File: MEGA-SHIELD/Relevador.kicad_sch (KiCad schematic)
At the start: 8 parts, among them J2 Conn_01x03_Female, J4 Screw_Terminal_01x04, K1 G5LE-1, Q1 2N7002H

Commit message: feat: cambios
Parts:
- R1: value 330 -> 1k
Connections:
- net sig: now reaches Q1.1 (G), R1.1, R3.1
- net 12V renamed +12V
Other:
- note removed: "aqui va el pin que usare para activar el relevador"
- moved on the sheet: D1, R1
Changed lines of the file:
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@@
 (kicad_sch (version 20230121) (generator eeschema)
   (paper "A4")
+  (junction (at 130.048 105.156) (diameter 0) (color 0 0 0 0)
+  )
   (junction (at 137.668 110.998) (diameter 0) (color 0 0 0 0)
   )
@@
   (junction (at 130.048 110.998) (diameter 0) (color 0 0 0 0)
   )
-  (junction (at 163.068 100.076) (diameter 0) (color 0 0 0 0)
-  )
-  (wire (pts (xy 101.6 110.998) (xy 106.172 110.998))
+  (wire (pts (xy 130.048 132.842) (xy 130.048 128.27))
     (stroke (width 0) (type default))
   )
@@
     (stroke (width 0) (type default))
   )
-  (wire (pts (xy 113.792 110.998) (xy 115.824 110.998))
+  (wire (pts (xy 127.254 105.156) (xy 130.048 105.156))
+    (stroke (width 0) (type default))
+  )
+  (wire (pts (xy 130.048 120.65) (xy 130.048 118.618))
     (stroke (width 0) (type default))
   )
@@
     (stroke (width 0) (type default))
   )
-  (wire (pts (xy 137.668 110.998) (xy 137.668 113.792))
+  (wire (pts (xy 137.668 110.998) (xy 137.668 132.08))
     (stroke (width 0) (type default))
   )
@@
     (stroke (width 0) (type default))
   )
-  (wire (pts (xy 123.444 110.998) (xy 130.048 110.998))
-    (stroke (width 0) (type default))
-  )
   (wire (pts (xy 142.748 81.788) (xy 142.748 87.122))
     (stroke (width 0) (type default))
   )
-  (wire (pts (xy 163.068 100.076) (xy 166.878 100.076))
-    (stroke (width 0) (type default))
-  )
   (wire (pts (xy 144.526 107.696) (xy 144.526 100.076))
     (stroke (width 0) (type default))
   )
-  (text "aqui va el pin que usare para activar el relevador "
-    (at 83.566 103.378 0)
-    (effects (font (size 1.27 1.27)) (justify left bottom))
-  )
-  (text "Relevador\n" (at 143.764 120.65 0)
+  (text "Relevador\n" (at 150.368 122.428 0)
     (effects (font (size 1.27 1.27) bold) (justify left bottom))
   )
-  (label "5v" (at 166.878 100.076 0) (fields_autoplaced)
-    (effects (font (size 1.27 1.27)) (justify left bottom))
-  )
-  (global_label "12V" (shape output) (at 142.748 81.788 180) (fields_autoplaced)
+  (hierarchical_label "sig" (shape input) (at 127.254 105.156 180) (fields_autoplaced)
     (effects (font (size 1.27 1.27)) (justify right))
-    (property "Intersheetrefs" "${INTERSHEET_REFS}" (at 136.3346 81.788 0)
-      (effects (font (size 1.27 1.27)) (justify right) hide)
-    )
-  )
-  (global_label "GND" (shape output) (at 101.6 110.998 180) (fields_autoplaced)
-    (effects (font (size 1.27 1.27)) (justify right))
-    (property "Intersheetrefs" "${INTERSHEET_REFS}" (at 94.8237 110.998 0)
-      (effects (font (size 1.27 1.27)) (justify right) hide)
-    )
-  )
-  (global_label "GND" (shape output) (at 172.974 101.346 0) (fields_autoplaced)
+  )
+  (hierarchical_label "5v" (shape input) (at 163.068 100.076 0) (fields_autoplaced)
     (effects (font (size 1.27 1.27)) (justify left))
-    (property "Intersheetrefs" "${INTERSHEET_REFS}" (at 179.7503 101.346 0)
-      (effects (font (size 1.27 1.27)) (justify left) hide)
-    )
-  )
-  (global_label "GND" (shape output) (at 137.668 113.792 0) (fields_autoplaced)
-    (effects (font (size 1.27 1.27)) (justify left))
-    (property "Intersheetrefs" "${INTERSHEET_REFS}" (at 144.4443 113.792 0)
-      (effects (font (size 1.27 1.27)) (justify left) hide)
+  )
+  (symbol (lib_id "power:GND") (at 130.048 132.842 0) (unit 1)
+    (in_bom yes) (on_board yes) (dnp no) (fields_autoplaced)
+    (property "Reference" "#PWR04" (at 130.048 139.192 0)
+      (effects (font (size 1.27 1.27)) hide)
+    )
+    (property "Value" "GND" (at 130.048 137.414 0)
+      (effects (font (size 1.27 1.27)))
+    )
+    (property "Footprint" "" (at 130.048 132.842 0)
+      (effects (font (size 1.27 1.27)) hide)
+    )
+    (property "Datasheet" "" (at 130.048 132.842 0)
+      (effects (font (size 1.27 1.27)) hide)
+    )
+    (pin "1")
+    (instances
+      (project "ER-PROMEGA-SHIELD"
+        (path "/8147067b-5845-4831-8ba1-364ec5fe594c/4fd23662-bc02-400a-9352-be1f3c09ed5b"
+          (reference "#PWR04") (unit 1)
+        )
+      )
     )
   )
@@
     )
   )
+  (symbol (lib_id "power:GND") (at 172.974 101.346 0) (unit 1)
+    (in_bom yes) (on_board yes) (dnp no) (fields_autoplaced)
+    (property "Reference" "#PWR02" (at 172.974 107.696 0)
+      (effects (font (size 1.27 1.27)) hide)
+    )
+    (property "Value" "GND" (at 172.974 106.68 0)
+      (effects (font (size 1.27 1.27)))
+    )
+    (property "Footprint" "" (at 172.974 101.346 0)
+      (effects (font (size 1.27 1.27)) hide)
+    )
+    (property "Datasheet" "" (at 172.974 101.346 0)
+      (effects (font (size 1.27 1.27)) hide)
+    )
+    (pin "1")
+    (instances
+      (project "ER-PROMEGA-SHIELD"
+        (path "/8147067b-5845-4831-8ba1-364ec5fe594c/4fd23662-bc02-400a-9352-be1f3c09ed5b"
+          (reference "#PWR02") (unit 1)
+        )
+      )
+    )
+  )
   (symbol (lib_id "Connector:Screw_Terminal_01x04") (at 178.054 89.916 0) (unit 1)
     (in_bom yes) (on_board yes) (dnp no)
@@
     )
   )
-  (symbol (lib_id "Device:R_US") (at 119.634 110.998 270) (unit 1)
-    (in_bom yes) (on_board yes) (dnp no)
-    (property "Reference" "R1" (at 118.364 107.95 90)
-      (effects (font (size 1.27 1.27)) (justify left))
-    )
-    (property "Value" "330" (at 118.11 105.156 90)
-      (effects (font (size 1.27 1.27)) (justify left))
-    )
-    (property "Footprint" "Resistor_SMD:R_0805_2012Metric_Pad1.20x1.40mm_HandSolder" (at 119.38 112.014 90)
-      (effects (font (size 1.27 1.27)) hide)
-    )
-    (property "Datasheet" "~" (at 119.634 110.998 0)
+  (symbol (lib_id "power:+12V") (at 142.748 81.788 0) (unit 1)
+    (in_bom yes) (on_board yes) (dnp no) (fields_autoplaced)
+    (property "Reference" "#PWR01" (at 142.748 85.598 0)
+      (effects (font (size 1.27 1.27)) hide)
+    )
+    (property "Value" "+12V" (at 142.748 76.454 0)
+      (effects (font (size 1.27 1.27)))
+    )
+    (property "Footprint" "" (at 142.748 81.788 0)
+      (effects (font (size 1.27 1.27)) hide)
+    )
+    (property "Datasheet" "" (at 142.748 81.788 0)
+      (effects (font (size 1.27 1.27)) hide)
+    )
+    (pin "1")
+    (instances
+      (project "ER-PROMEGA-SHIELD"
+        (path "/8147067b-5845-4831-8ba1-364ec5fe594c/4fd23662-bc02-400a-9352-be1f3c09ed5b"
+          (reference "#PWR01") (unit 1)
+        )
+      )
+    )
+  )
+  (symbol (lib_id "Device:R_US") (at 130.048 114.808 0) (unit 1)
+    (in_bom yes) (on_board yes) (dnp no)
+    (property "Reference" "R1" (at 124.714 113.284 0)
+      (effects (font (size 1.27 1.27)) (justify left))
+    )
+    (property "Value" "1k" (at 124.968 115.316 0)
+      (effects (font (size 1.27 1.27)) (justify left))
+    )
+    (property "Footprint" "Resistor_SMD:R_0805_2012Metric_Pad1.20x1.40mm_HandSolder" (at 131.064 115.062 90)
+      (effects (font (size 1.27 1.27)) hide)
+    )
+    (property "Datasheet" "~" (at 130.048 114.808 0)
       (effects (font (size 1.27 1.27)) hide)
     )
@@
     )
   )
-  (symbol (lib_id "Device:LED") (at 109.982 110.998 0) (unit 1)
-    (in_bom yes) (on_board yes) (dnp no)
-    (property "Reference" "D1" (at 109.22 107.696 0)
+  (symbol (lib_id "Device:LED") (at 130.048 124.46 90) (unit 1)
+    (in_bom yes) (on_board yes) (dnp no)
+    (property "Reference" "D1" (at 123.952 123.19 90)
       (effects (font (size 1.27 1.27)) (justify right))
     )
-    (property "Value" "LEDRELE" (at 112.014 115.57 0)
+    (property "Value" "LEDRELE" (at 120.396 125.984 90)
       (effects (font (size 1.27 1.27)) (justify right))
     )
-    (property "Footprint" "LED_SMD:LED_1206_3216Metric_Pad1.42x1.75mm_HandSolder" (at 109.982 110.998 0)
-      (effects (font (size 1.27 1.27)) hide)
-    )
-    (property "Datasheet" "~" (at 109.982 110.998 0)
+    (property "Footprint" "LED_SMD:LED_1206_3216Metric_Pad1.42x1.75mm_HandSolder" (at 130.048 124.46 0)
+      (effects (font (size 1.27 1.27)) hide)
+    )
+    (property "Datasheet" "~" (at 130.048 124.46 0)
       (effects (font (size 1.27 1.27)) hide)
     )
@@
         )
       )
+    )
+  )
+  (symbol (lib_id "power:GND") (at 137.668 132.08 0) (unit 1)
+    (in_bom yes) (on_board yes) (dnp no) (fields_autoplaced)
+    (property "Reference" "#PWR03" (at 137.668 138.43 0)
+      (effects (font (size 1.27 1.27)) hide)
+    )
+    (property "Value" "GND" (at 137.668 136.906 0)
+      (effects (font (size 1.27 1.27)))
+    )
+    (property "Footprint" "" (at 137.668 132.08 0)
+      (effects (font (size 1.27 1.27)) hide)
+    )
+    (property "Datasheet" "" (at 137.668 132.08 0)
+      (effects (font (size 1.27 1.27)) hide)
+    )
+    (pin "1")
+    (instances
+      (project "ER-PROMEGA-SHIELD"
+        (path "/8147067b-5845-4831-8ba1-364ec5fe594c/4fd23662-bc02-400a-9352-be1f3c09ed5b"
+          (reference "#PWR03") (unit 1)
+        )
+      )

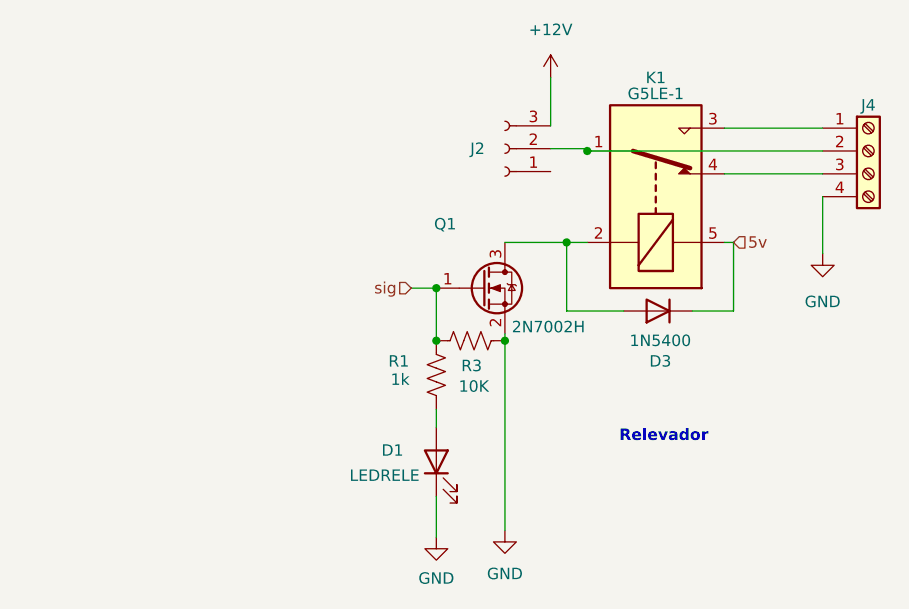
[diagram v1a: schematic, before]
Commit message: feat: agrege reles y optos
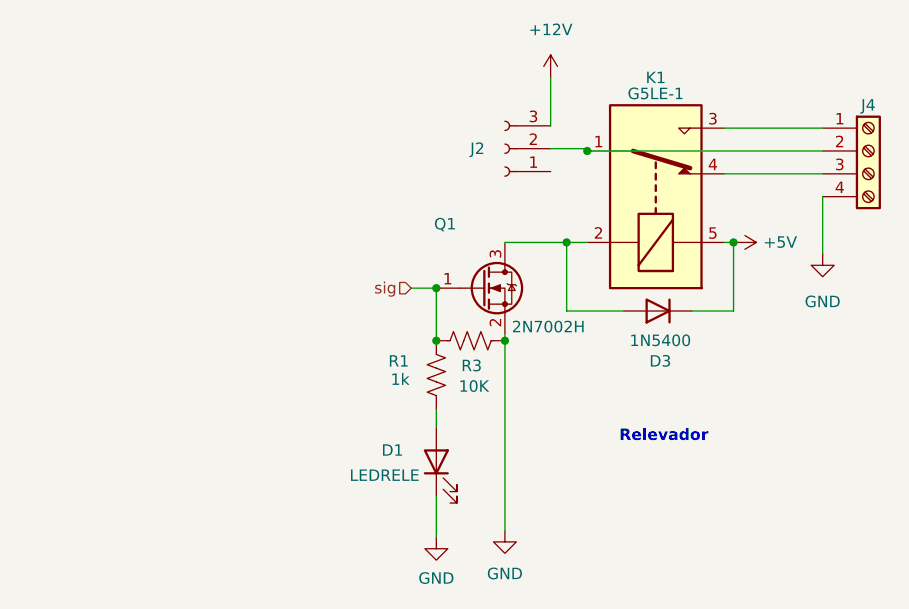
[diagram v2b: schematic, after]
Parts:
- J4: footprint Connector_Phoenix_MC:PhoenixContact_MC_1,5_4-G-3.81_1x04_P3.81mm_Horizontal -> TerminalBlock_Phoenix:TerminalBlock_Phoenix_MPT-0,5-4-2.54_1x04_P2.54mm_Horizontal
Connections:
- net 5v renamed +5V
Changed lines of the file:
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@@
   (junction (at 146.812 89.916) (diameter 0) (color 0 0 0 0)
+  )
+  (junction (at 163.068 100.076) (diameter 0) (color 0 0 0 0)
   )
   (junction (at 144.526 100.076) (diameter 0) (color 0 0 0 0)
@@
   (hierarchical_label "sig" (shape input) (at 127.254 105.156 180) (fields_autoplaced)
     (effects (font (size 1.27 1.27)) (justify right))
-  )
-  (hierarchical_label "5v" (shape input) (at 163.068 100.076 0) (fields_autoplaced)
-    (effects (font (size 1.27 1.27)) (justify left))
   )
   (symbol (lib_id "power:GND") (at 130.048 132.842 0) (unit 1)
@@
           (reference "#PWR04") (unit 1)
         )
+        (path "/8147067b-5845-4831-8ba1-364ec5fe594c/0e8259b0-292b-460c-945a-11bb3aca89bc"
+          (reference "#PWR014") (unit 1)
+        )
+        (path "/8147067b-5845-4831-8ba1-364ec5fe594c/aef94730-93c3-47e2-8928-ca20750b33d8"
+          (reference "#PWR019") (unit 1)
+        )
+        (path "/8147067b-5845-4831-8ba1-364ec5fe594c/789afc0a-eb2f-4f7b-9922-dc73cde413f6"
+          (reference "#PWR024") (unit 1)
+        )
       )
     )
@@
         (path "/8147067b-5845-4831-8ba1-364ec5fe594c/4fd23662-bc02-400a-9352-be1f3c09ed5b"
           (reference "R5") (unit 1)
+        )
+        (path "/8147067b-5845-4831-8ba1-364ec5fe594c/0e8259b0-292b-460c-945a-11bb3aca89bc"
+          (reference "R7") (unit 1)
+        )
+        (path "/8147067b-5845-4831-8ba1-364ec5fe594c/aef94730-93c3-47e2-8928-ca20750b33d8"
+          (reference "R9") (unit 1)
+        )
+        (path "/8147067b-5845-4831-8ba1-364ec5fe594c/789afc0a-eb2f-4f7b-9922-dc73cde413f6"
+          (reference "R11") (unit 1)
         )
       )
@@
         (path "/8147067b-5845-4831-8ba1-364ec5fe594c/4fd23662-bc02-400a-9352-be1f3c09ed5b"
           (reference "Q1") (unit 1)
+        )
+        (path "/8147067b-5845-4831-8ba1-364ec5fe594c/0e8259b0-292b-460c-945a-11bb3aca89bc"
+          (reference "Q2") (unit 1)
+        )
+        (path "/8147067b-5845-4831-8ba1-364ec5fe594c/aef94730-93c3-47e2-8928-ca20750b33d8"
+          (reference "Q3") (unit 1)
+        )
+        (path "/8147067b-5845-4831-8ba1-364ec5fe594c/789afc0a-eb2f-4f7b-9922-dc73cde413f6"
+          (reference "Q4") (unit 1)
         )
       )
@@
           (reference "K1") (unit 1)
         )
+        (path "/8147067b-5845-4831-8ba1-364ec5fe594c/0e8259b0-292b-460c-945a-11bb3aca89bc"
+          (reference "K2") (unit 1)
+        )
+        (path "/8147067b-5845-4831-8ba1-364ec5fe594c/aef94730-93c3-47e2-8928-ca20750b33d8"
+          (reference "K3") (unit 1)
+        )
+        (path "/8147067b-5845-4831-8ba1-364ec5fe594c/789afc0a-eb2f-4f7b-9922-dc73cde413f6"
+          (reference "K4") (unit 1)
+        )
       )
     )
@@
           (reference "#PWR02") (unit 1)
         )
+        (path "/8147067b-5845-4831-8ba1-364ec5fe594c/0e8259b0-292b-460c-945a-11bb3aca89bc"
+          (reference "#PWR018") (unit 1)
+        )
+        (path "/8147067b-5845-4831-8ba1-364ec5fe594c/aef94730-93c3-47e2-8928-ca20750b33d8"
+          (reference "#PWR023") (unit 1)
+        )
+        (path "/8147067b-5845-4831-8ba1-364ec5fe594c/789afc0a-eb2f-4f7b-9922-dc73cde413f6"
+          (reference "#PWR028") (unit 1)
+        )
       )
     )
@@
       (effects (font (size 1.27 1.27)) hide)
     )
-    (property "Footprint" "Connector_Phoenix_MC:PhoenixContact_MC_1,5_4-G-3.81_1x04_P3.81mm_Horizontal" (at 178.054 89.916 0)
+    (property "Footprint" "TerminalBlock_Phoenix:TerminalBlock_Phoenix_MPT-0,5-4-2.54_1x04_P2.54mm_Horizontal" (at 178.054 89.916 0)
       (effects (font (size 1.27 1.27)) hide)
     )
@@
         (path "/8147067b-5845-4831-8ba1-364ec5fe594c/4fd23662-bc02-400a-9352-be1f3c09ed5b"
           (reference "J3") (unit 1)
+        )
+        (path "/8147067b-5845-4831-8ba1-364ec5fe594c/0e8259b0-292b-460c-945a-11bb3aca89bc"
+          (reference "J13") (unit 1)
+        )
+        (path "/8147067b-5845-4831-8ba1-364ec5fe594c/aef94730-93c3-47e2-8928-ca20750b33d8"
+          (reference "J15") (unit 1)
+        )
+        (path "/8147067b-5845-4831-8ba1-364ec5fe594c/789afc0a-eb2f-4f7b-9922-dc73cde413f6"
+          (reference "J17") (unit 1)
         )
       )
@@
           (reference "#PWR01") (unit 1)
         )
+        (path "/8147067b-5845-4831-8ba1-364ec5fe594c/0e8259b0-292b-460c-945a-11bb3aca89bc"
+          (reference "#PWR016") (unit 1)
+        )
+        (path "/8147067b-5845-4831-8ba1-364ec5fe594c/aef94730-93c3-47e2-8928-ca20750b33d8"
+          (reference "#PWR021") (unit 1)
+        )
+        (path "/8147067b-5845-4831-8ba1-364ec5fe594c/789afc0a-eb2f-4f7b-9922-dc73cde413f6"
+          (reference "#PWR026") (unit 1)
+        )
       )
     )
@@
           (reference "R4") (unit 1)
         )
+        (path "/8147067b-5845-4831-8ba1-364ec5fe594c/0e8259b0-292b-460c-945a-11bb3aca89bc"
+          (reference "R6") (unit 1)
+        )
+        (path "/8147067b-5845-4831-8ba1-364ec5fe594c/aef94730-93c3-47e2-8928-ca20750b33d8"
+          (reference "R8") (unit 1)
+        )
+        (path "/8147067b-5845-4831-8ba1-364ec5fe594c/789afc0a-eb2f-4f7b-9922-dc73cde413f6"
+          (reference "R10") (unit 1)
+        )
       )
     )
@@
         (path "/8147067b-5845-4831-8ba1-364ec5fe594c/4fd23662-bc02-400a-9352-be1f3c09ed5b"
           (reference "J2") (unit 1)
+        )
+        (path "/8147067b-5845-4831-8ba1-364ec5fe594c/0e8259b0-292b-460c-945a-11bb3aca89bc"
+          (reference "J12") (unit 1)
+        )
+        (path "/8147067b-5845-4831-8ba1-364ec5fe594c/aef94730-93c3-47e2-8928-ca20750b33d8"
+          (reference "J14") (unit 1)
+        )
+        (path "/8147067b-5845-4831-8ba1-364ec5fe594c/789afc0a-eb2f-4f7b-9922-dc73cde413f6"
+          (reference "J16") (unit 1)
         )
       )
@@
           (reference "D3") (unit 1)
         )
+        (path "/8147067b-5845-4831-8ba1-364ec5fe594c/0e8259b0-292b-460c-945a-11bb3aca89bc"
+          (reference "D5") (unit 1)
+        )
+        (path "/8147067b-5845-4831-8ba1-364ec5fe594c/aef94730-93c3-47e2-8928-ca20750b33d8"
+          (reference "D7") (unit 1)
+        )
+        (path "/8147067b-5845-4831-8ba1-364ec5fe594c/789afc0a-eb2f-4f7b-9922-dc73cde413f6"
+          (reference "D9") (unit 1)
+        )
       )
     )
@@
         (path "/8147067b-5845-4831-8ba1-364ec5fe594c/4fd23662-bc02-400a-9352-be1f3c09ed5b"
           (reference "D4") (unit 1)
+        )
+        (path "/8147067b-5845-4831-8ba1-364ec5fe594c/0e8259b0-292b-460c-945a-11bb3aca89bc"
+          (reference "D6") (unit 1)
+        )
+        (path "/8147067b-5845-4831-8ba1-364ec5fe594c/aef94730-93c3-47e2-8928-ca20750b33d8"
+          (reference "D8") (unit 1)
+        )
+        (path "/8147067b-5845-4831-8ba1-364ec5fe594c/789afc0a-eb2f-4f7b-9922-dc73cde413f6"
+          (reference "D10") (unit 1)
         )
       )
@@
           (reference "#PWR03") (unit 1)
         )
-      )
+        (path "/8147067b-5845-4831-8ba1-364ec5fe594c/0e8259b0-292b-460c-945a-11bb3aca89bc"
+          (reference "#PWR015") (unit 1)
+        )
+        (path "/8147067b-5845-4831-8ba1-364ec5fe594c/aef94730-93c3-47e2-8928-ca20750b33d8"
+          (reference "#PWR020") (unit 1)
+        )
+        (path "/8147067b-5845-4831-8ba1-364ec5fe594c/789afc0a-eb2f-4f7b-9922-dc73cde413f6"
+          (reference "#PWR025") (unit 1)
+        )
+      )
+    )
+  )
+  (symbol (lib_id "power:+5V") (at 163.068 100.076 270) (unit 1)
+    (in_bom yes) (on_board yes) (dnp no) (fields_autoplaced)
+    (property "Reference" "#PWR013" (at 159.258 100.076 0)
+      (effects (font (size 1.27 1.27)) hide)
+    )
+    (property "Value" "+5V" (at 166.37 100.076 90)
+      (effects (font (size 1.27 1.27)) (justify left))
+    )
+    (property "Footprint" "" (at 163.068 100.076 0)
+      (effects (font (size 1.27 1.27)) hide)
+    )
+    (property "Datasheet" "" (at 163.068 100.076 0)
+      (effects (font (size 1.27 1.27)) hide)
+    )
+    (pin "1")
+    (instances
+      (project "ER-PROMEGA-SHIELD"
+        (path "/8147067b-5845-4831-8ba1-364ec5fe594c/4fd23662-bc02-400a-9352-be1f3c09ed5b"
+          (reference "#PWR013") (unit 1)
+        )
+        (path "/8147067b-5845-4831-8ba1-364ec5fe594c/0e8259b0-292b-460c-945a-11bb3aca89bc"
+          (reference "#PWR017") (unit 1)
+        )
+        (path "/8147067b-5845-4831-8ba1-364ec5fe594c/aef94730-93c3-47e2-8928-ca20750b33d8"
+          (reference "#PWR022") (unit 1)
+        )
+        (path "/8147067b-5845-4831-8ba1-364ec5fe594c/789afc0a-eb2f-4f7b-9922-dc73cde413f6"
+          (reference "#PWR027") (unit 1)
+        )
+      )
